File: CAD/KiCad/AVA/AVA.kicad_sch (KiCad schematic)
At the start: 48 parts, among them J1 Conn_01x03_Pin, J10 Conn_01x04_Pin, J2 Conn_01x03_Pin, J3 Conn_01x03_Pin, J4 Conn_01x03_Pin, J5 Conn_01x02_Pin, J6 Conn_01x02_Pin, J7 Conn_01x02_Pin, J8 Conn_01x03_Pin, J9 Conn_01x03_Pin, U1 WEMOS_C3_mini

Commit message: README doesn't include PDF apparently
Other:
- title: (none) -> AVA
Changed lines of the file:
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@@
 	(generator_version "10.0")
 	(paper "A4")
+	(title_block
+		(title "AVA")
+		(date "0026-04-28")
+		(rev "0")
+	)
 	(text_box "Hall #2"
 		(exclude_from_sim no)

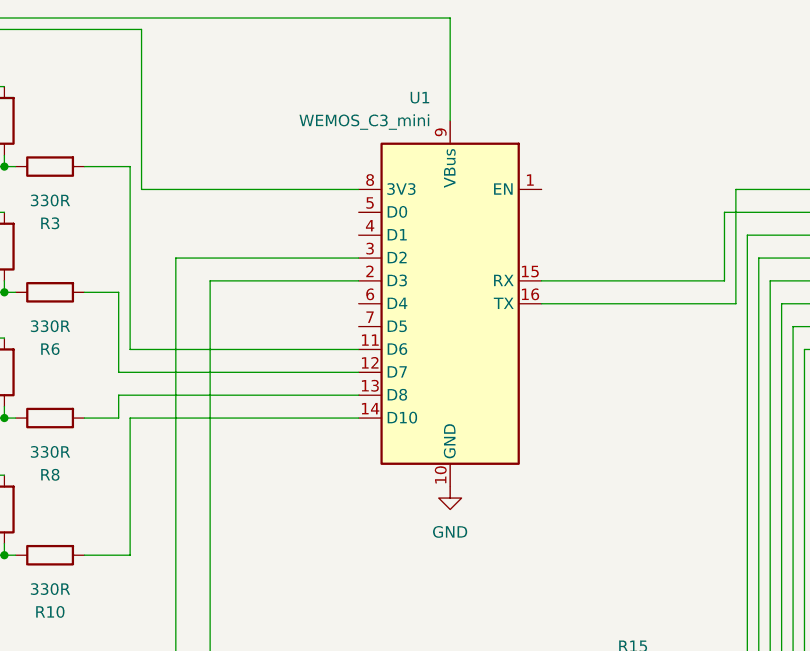
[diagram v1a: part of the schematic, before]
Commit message: Slight changes for layout necessary. We've a ESP32-C3-Super-Mini, not an ESP32-C3-Mini. Completely different pinout and footprint. Watch me add a custom footprint and blow my shit smooth off
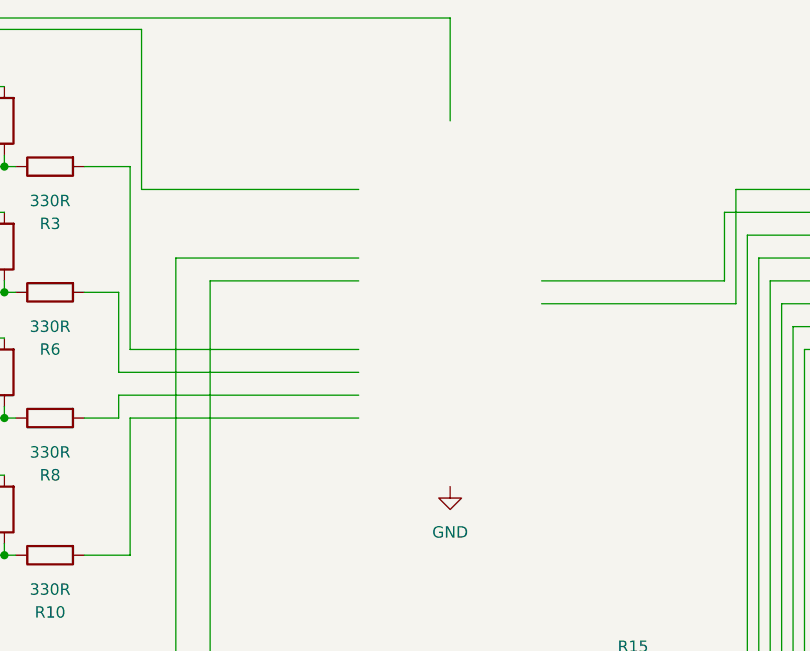
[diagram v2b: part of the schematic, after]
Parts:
- removed U1: WEMOS_C3_mini, RF_Module:WEMOS_C3_mini, symbol RF_Module:WEMOS_C3_mini
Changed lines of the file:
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@@
-	)
-	(symbol
-		(lib_id "RF_Module:WEMOS_C3_mini")
-		(at 134.62 58.42 0)
-		(mirror y)
-		(unit 1)
-		(body_style 1)
-		(exclude_from_sim no)
-		(in_bom yes)
-		(on_board yes)
-		(in_pos_files yes)
-		(dnp no)
-		(property "Reference" "U1"
-			(at 132.4591 35.56 0)
-			(show_name no)
-			(do_not_autoplace no)
-			(effects
-				(font
-					(size 1.27 1.27)
-				)
-				(justify left)
-			)
-		)
-		(property "Value" "WEMOS_C3_mini"
-			(at 132.4591 38.1 0)
-			(show_name no)
-			(do_not_autoplace no)
-			(effects
-				(font
-					(size 1.27 1.27)
-				)
-				(justify left)
-			)
-		)
-		(property "Footprint" "RF_Module:WEMOS_C3_mini"
-			(at 134.62 87.63 0)
-			(hide yes)
-			(show_name no)
-			(do_not_autoplace no)
-			(effects
-				(font
-					(size 1.27 1.27)
-				)
-			)
-		)
-		(property "Datasheet" "https://www.wemos.cc/en/latest/c3/c3_mini.html"
-			(at 134.62 84.836 0)
-			(hide yes)
-			(show_name no)
-			(do_not_autoplace no)
-			(effects
-				(font
-					(size 1.27 1.27)
-				)
-			)
-		)
-		(property "Description" "32-bit microcontroller module with WiFi"
-			(at 133.858 81.534 0)
-			(hide yes)
-			(show_name no)
-			(do_not_autoplace no)
-			(effects
-				(font
-					(size 1.27 1.27)
-				)
-			)
-		)
-		(pin "10"
-		)
-		(pin "14"
-		)
-		(pin "8"
-		)
-		(pin "1"
-		)
-		(pin "12"
-		)
-		(pin "11"
-		)
-		(pin "13"
-		)
-		(pin "15"
-		)
-		(pin "9"
-		)
-		(pin "2"
-		)
-		(pin "6"
-		)
-		(pin "5"
-		)
-		(pin "16"
-		)
-		(pin "3"
-		)
-		(pin "7"
-		)
-		(pin "4"
-		)
-		(instances
-			(project "AVA"
-				(path "/3a21ef45-a289-4ca0-a48e-1dc6434e5bcf"
-					(reference "U1")
-					(unit 1)
-				)
-			)
-		)
 	)
 	(symbol

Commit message: Using correct footprint now. Jarvis, more alcohol
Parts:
- added U1: (no value), AVA:ESP32-C3-Super-Mini, symbol AVA:ESP32-C3-SuperMini
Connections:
- net GND: now also U1.15 (GND)
- net at C1.1, C2.1, C3.1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: now also U1.16 (5V)
- net at C6.2, R13.2, R14.2: now also U1.5 (D9)
- net at R1.1: now also U1.7 (RX)
- net at C5.2, R11.2, R12.2: now also U1.6 (D10)
- net at R8.2: now also U1.10 (D1)
- net at R10.2: now also U1.9 (D0)
- net at R2.1: now also U1.8 (TX)
- net at R4.2, R5.2, R7.2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: now also U1.14 (3.3V)
- net at R3.2: now also U1.12 (D3)
- net at R6.2: now also U1.11 (D2)

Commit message: Track width min now 1.6mm. Double sided board, no pre-drawn holes in front, back svg for easy printing
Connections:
- net VCC: now reaches C1.1, C2.1, C3.1, C4.1, J1.1 (Pin_1), J2.1 (Pin_1), J3.1 (Pin_1), J4.1 (Pin_1), U1.16 (5V)
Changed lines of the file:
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@@
+	)
+	(junction
+		(at 125.73 26.67)
+		(diameter 0)
+		(color 0 0 0 0)
 	)
 	(junction
@@
 					(unit 1)
 				)
+			)
+		)
+	)
+	(symbol
+		(lib_id "power:VCC")
+		(at 125.73 26.67 270)
+		(unit 1)
+		(body_style 1)
+		(exclude_from_sim no)
+		(in_bom yes)
+		(on_board yes)
+		(in_pos_files yes)
+		(dnp no)
+		(fields_autoplaced yes)
+		(property "Reference" "#PWR017"
+			(at 121.92 26.67 0)
+			(hide yes)
+			(show_name no)
+			(do_not_autoplace no)
+			(effects
+				(font
+					(size 1.27 1.27)
+				)
+			)
+		)
+		(property "Value" "VCC"
+			(at 129.54 26.67 90)
+			(show_name no)
+			(do_not_autoplace no)
+			(effects
+				(font
+					(size 1.27 1.27)
+				)
+				(justify left)
+			)
+		)
+		(property "Footprint" ""
+			(at 125.73 26.67 0)
+			(hide yes)
+			(show_name no)
+			(do_not_autoplace no)
+			(effects
+				(font
+					(size 1.27 1.27)
+				)
+			)
+		)
+		(property "Datasheet" ""
+			(at 125.73 26.67 0)
+			(hide yes)
+			(show_name no)
+			(do_not_autoplace no)
+			(effects
+				(font
+					(size 1.27 1.27)
+				)
+			)
+		)
+		(property "Description" "Power symbol creates a global label with name \"VCC\""
+			(at 125.73 26.67 0)
+			(hide yes)
+			(show_name no)
+			(do_not_autoplace no)
+			(effects
+				(font
+					(size 1.27 1.27)
+				)
+			)
+		)
+		(pin "1"
+		)
+		(instances
+			(project "AVA"
+				(path "/3a21ef45-a289-4ca0-a48e-1dc6434e5bcf"
+					(reference "#PWR017")
+					(unit 1)
+				)

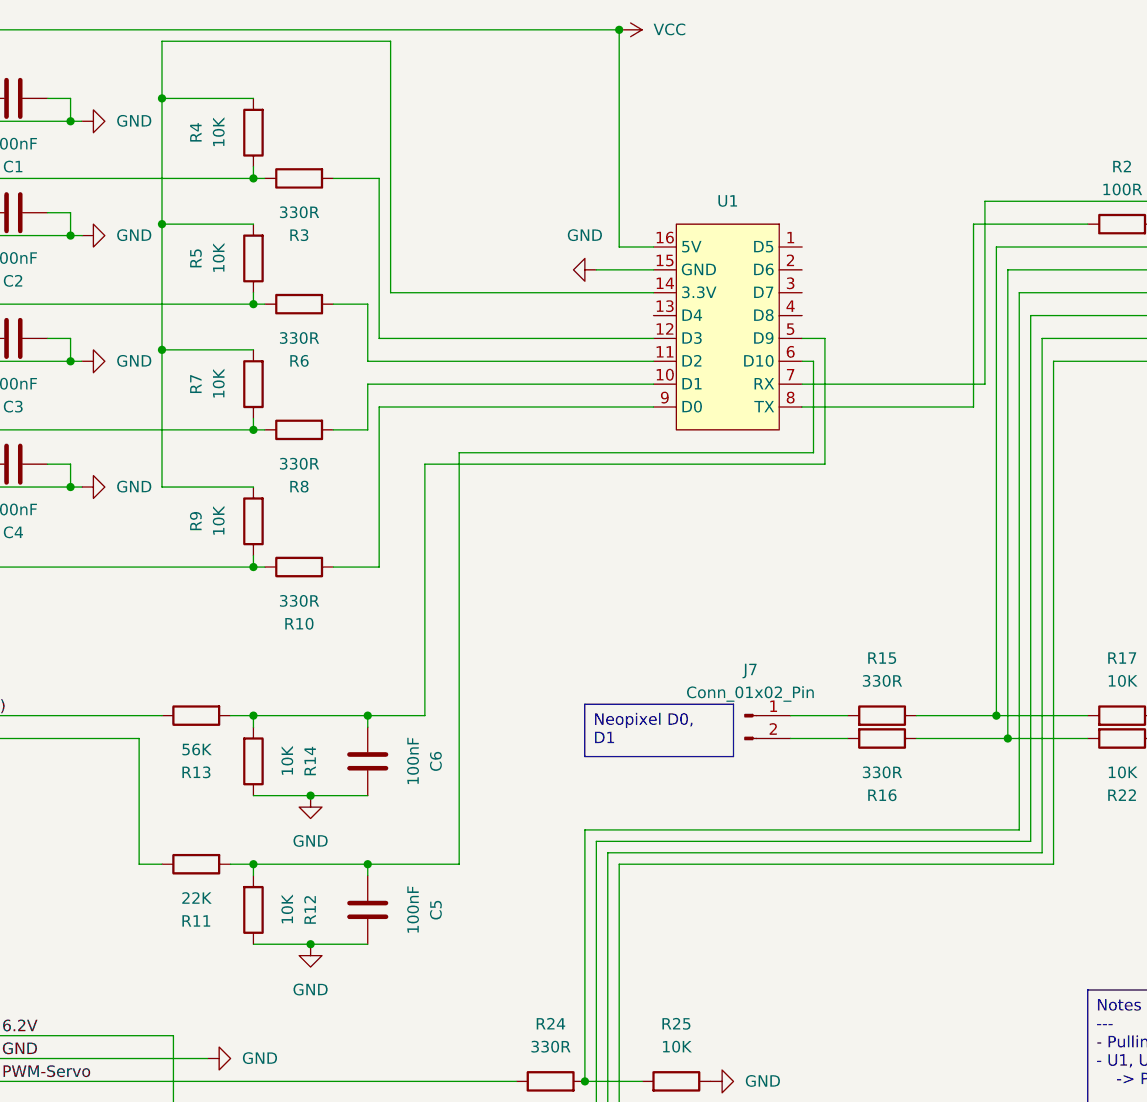
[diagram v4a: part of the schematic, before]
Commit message: ESP32-C3-SuperMini and Arduino Nano ESP32 layout. Next variant ESP32-C3-SuperMini and ESP32-WROOM-32U
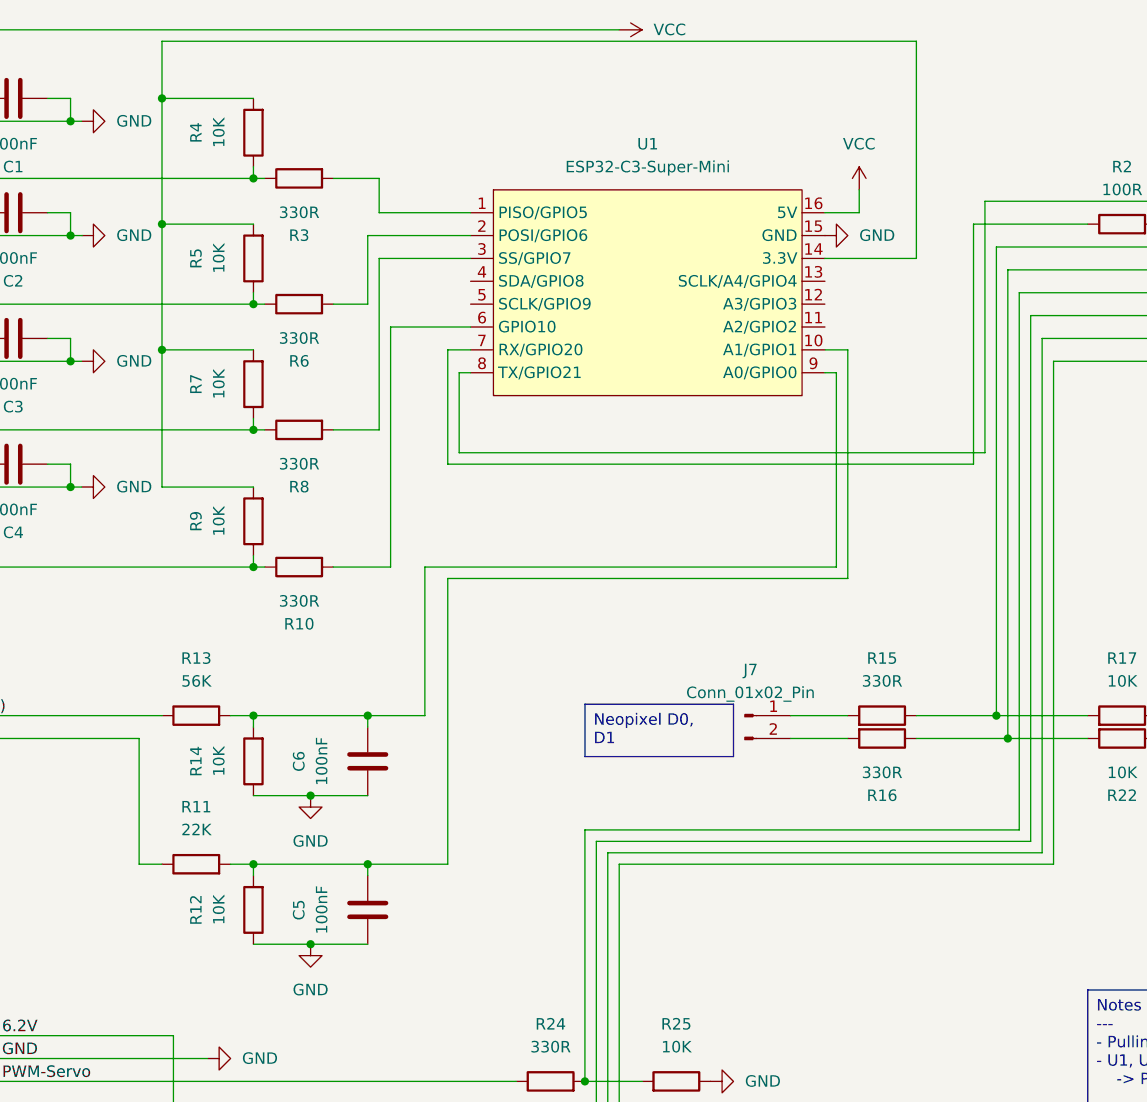
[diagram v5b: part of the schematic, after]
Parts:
- U1: value (none) -> ESP32-C3-Super-Mini
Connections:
- net at U1.1 (PISO/GPIO5): now also R3.2
- net at U1.10 (A1/GPIO1): now also C5.2, R11.2, R12.2; no longer R8.2
- net at U1.11 (A2/GPIO2): no longer R6.2
- net at U1.12 (A3/GPIO3): no longer R3.2
- net at U1.2 (POSI/GPIO6): now also R6.2
- net at U1.3 (SS/GPIO7): now also R8.2
- net at C6.2, R13.2, R14.2: now also U1.9 (A0/GPIO0); no longer U1.5 (D9)
- net at R1.1: now also U1.8 (TX/GPIO21); no longer U1.7 (RX)
- net at R2.1: now also U1.7 (RX/GPIO20); no longer U1.8 (TX)
- net at R10.2: now also U1.6 (GPIO10); no longer U1.9 (D0)
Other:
- moved on the sheet: C5, C6, R12, R14

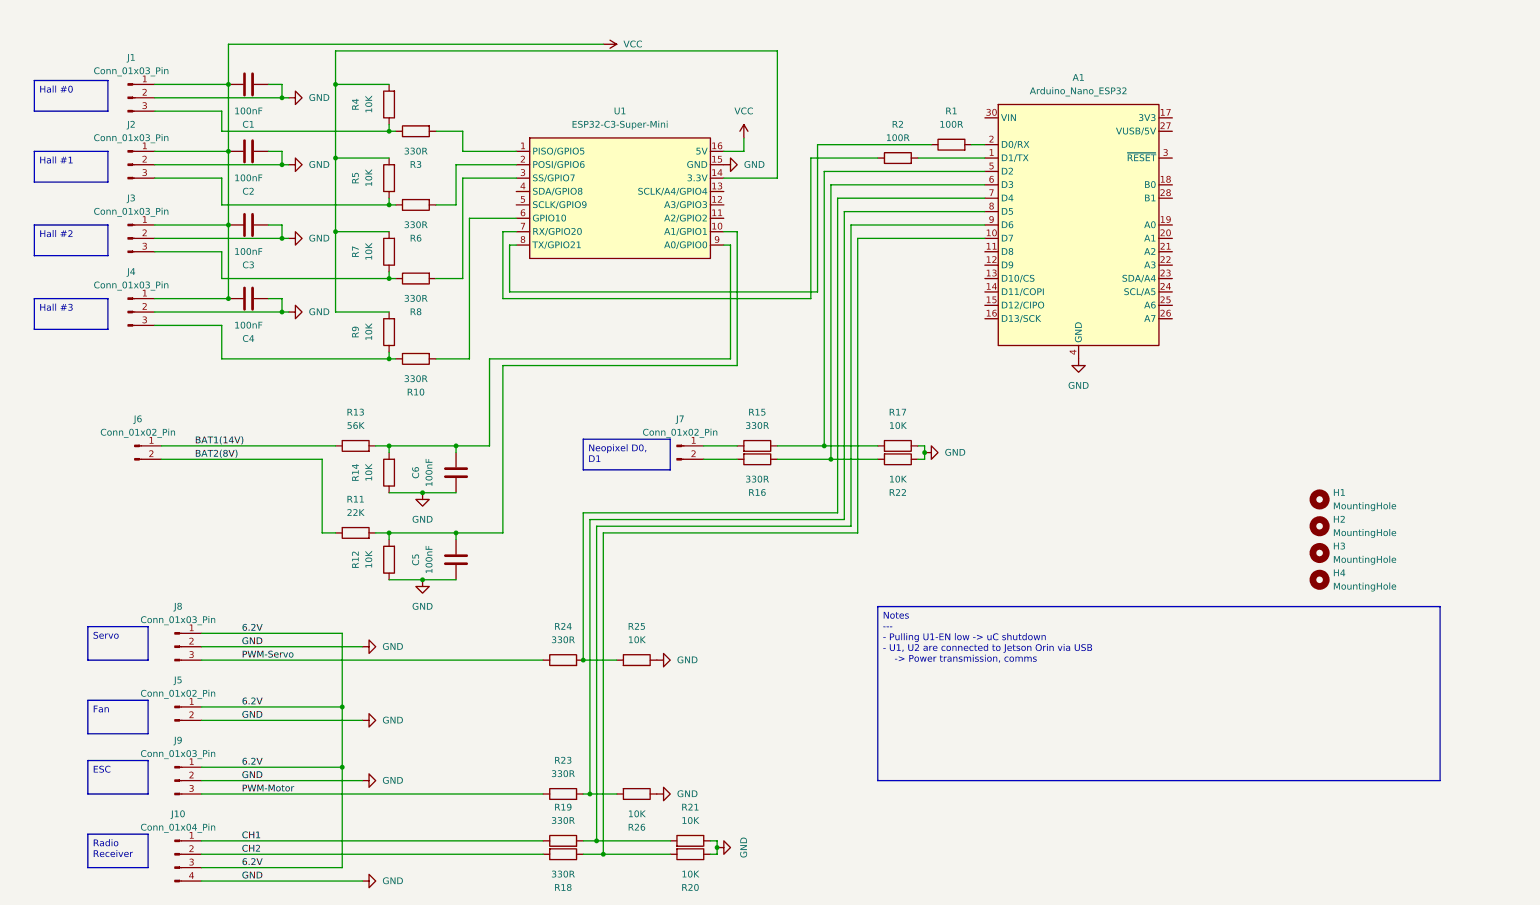
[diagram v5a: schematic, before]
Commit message: Updated schematic for new ESP32-WROOM-DEVKIT
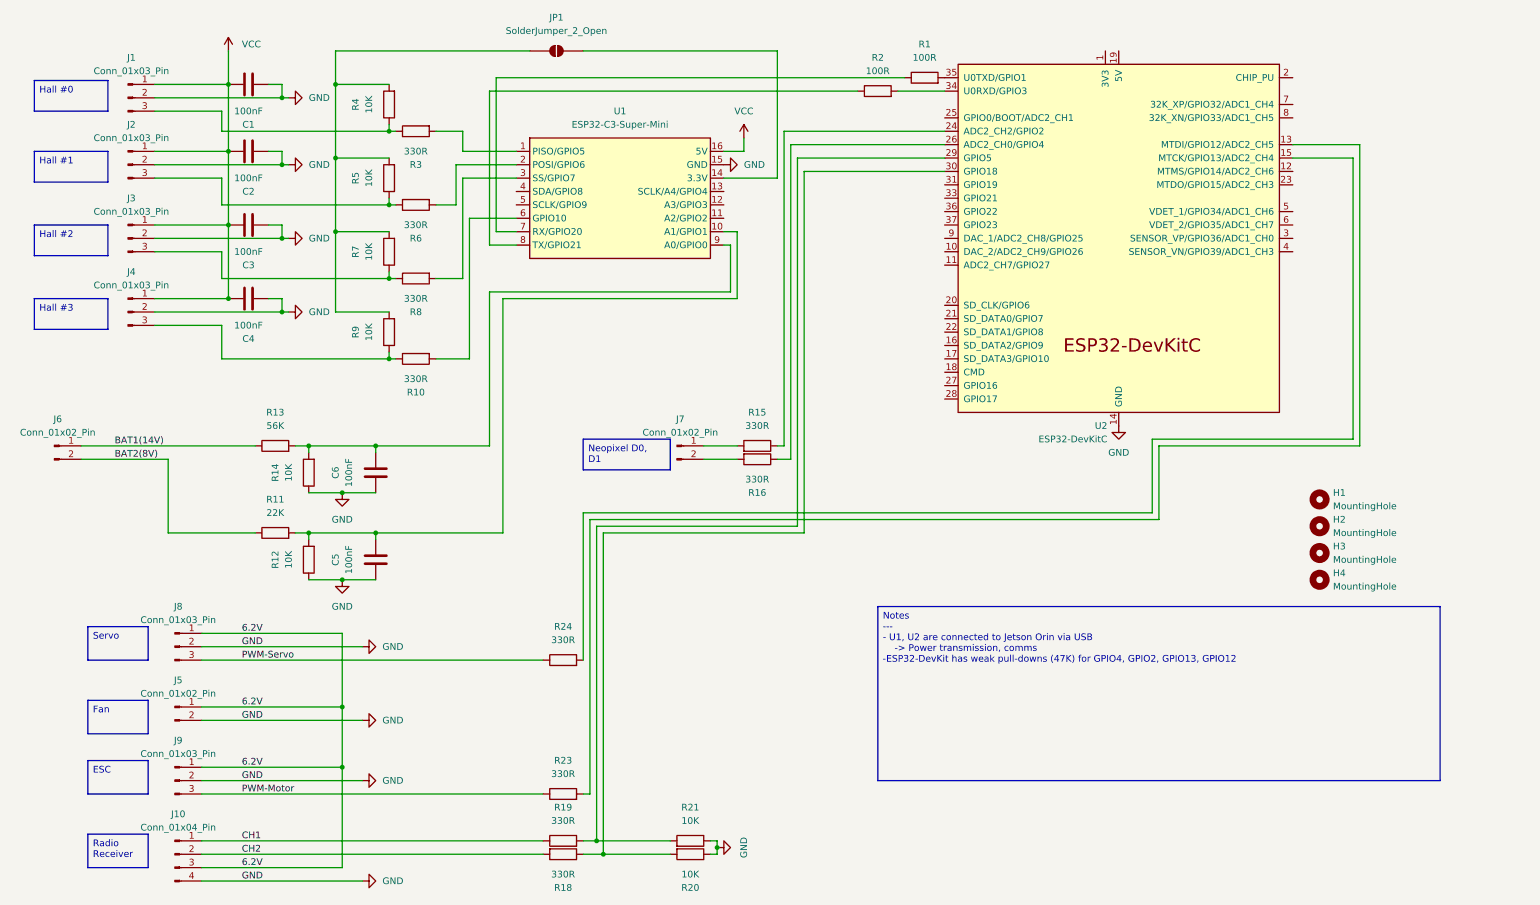
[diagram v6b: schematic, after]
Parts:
- removed A1: Arduino_Nano_ESP32, Module:Arduino_Nano, symbol MCU_Module:Arduino_Nano_ESP32
- removed R17, R22, R25, R26: 10K, Resistor_THT:R_Axial_DIN0207_L6.3mm_D2.5mm_P10.16mm_Horizontal, symbol Device:R
- added JP1: SolderJumper_2_Open, Jumper:SolderJumper-2_P1.3mm_Open_RoundedPad1.0x1.5mm, symbol Jumper:SolderJumper_2_Open
- added U2: ESP32-DevKitC, PCM_Espressif:ESP32-DevKitC, symbol PCM_Espressif:ESP32-DevKitC
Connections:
- net GND: now also U2.14 (GND), U2.32 (GND), U2.38 (GND)
- net at R16.1: now also U2.26 (ADC2_CH0/GPIO4)
- net at R24.2: now also U2.15 (MTCK/GPIO13/ADC2_CH4)
- net at R18.1, R20.2: now also U2.30 (GPIO18)
- net at R15.1: now also U2.24 (ADC2_CH2/GPIO2)
- net at R1.1: now also U1.7 (RX/GPIO20); no longer U1.8 (TX/GPIO21)
- net at R1.2: now also U2.35 (U0TXD/GPIO1)
- net at R2.2: now also U2.34 (U0RXD/GPIO3)
- net at R23.2: now also U2.13 (MTDI/GPIO12/ADC2_CH5)
- net at R19.2, R21.2: now also U2.29 (GPIO5)
- net at R4.2, R5.2, R7.2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: now also JP1.1 (A); no longer U1.14 (3.3V)
- net at R2.1: now also U1.8 (TX/GPIO21); no longer U1.7 (RX/GPIO20)
- new net: JP1.2 (B), U1.14 (3.3V)
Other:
- moved on the sheet: C5, C6, J6, R1, R11, R12, R13, R14, R2

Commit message: :D
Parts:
- removed JP1: SolderJumper_2_Open, Jumper:SolderJumper-2_P1.3mm_Open_RoundedPad1.0x1.5mm, symbol Jumper:SolderJumper_2_Open
- added R22, R25, R26, R27: 10K, Resistor_THT:R_Axial_DIN0207_L6.3mm_D2.5mm_P10.16mm_Horizontal, symbol Device:R
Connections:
- net GND: now also R22.1, R25.1, R26.1, R27.1
- net PWM-Servo: now also R24.2; no longer R24.1
- net at U2.15 (MTCK/GPIO13/ADC2_CH4): no longer R24.2
- net at R18.1, R20.2: now also U2.37 (GPIO23); no longer U2.30 (GPIO18)
- net at R4.2, R5.2, R7.2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: now also U1.14 (3.3V)
- net at R8.2: now also U1.12 (A3/GPIO3); no longer U1.3 (SS/GPIO7)
- net at R10.2: now also U1.13 (SCLK/A4/GPIO4); no longer U1.6 (GPIO10)
- net at R15.1: now also U2.29 (GPIO5), R26.2; no longer U2.24 (ADC2_CH2/GPIO2)
- net at R19.2, R21.2: now also U2.36 (GPIO22); no longer U2.29 (GPIO5)
- net at U1.11 (A2/GPIO2): now also R6.2
- net at U1.2 (POSI/GPIO6): no longer R6.2
- net at R23.2: now also U2.33 (GPIO21), R22.2; no longer U2.13 (MTDI/GPIO12/ADC2_CH5)
- net at U2.26 (ADC2_CH0/GPIO4): no longer R16.1
- net at U2.31 (GPIO19): now also R24.1, R25.2
- new net: R16.1, R27.2, U2.30 (GPIO18)
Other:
- moved on the sheet: R24
